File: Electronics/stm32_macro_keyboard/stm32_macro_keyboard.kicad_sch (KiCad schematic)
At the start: 37 parts, among them J1 USB_B_Micro, J2 Conn_01x04_Pin, SW1 SW_SPDT, U1 STM32F072CBTx, U2 AMS1117-3.3, Y1 16 MHz

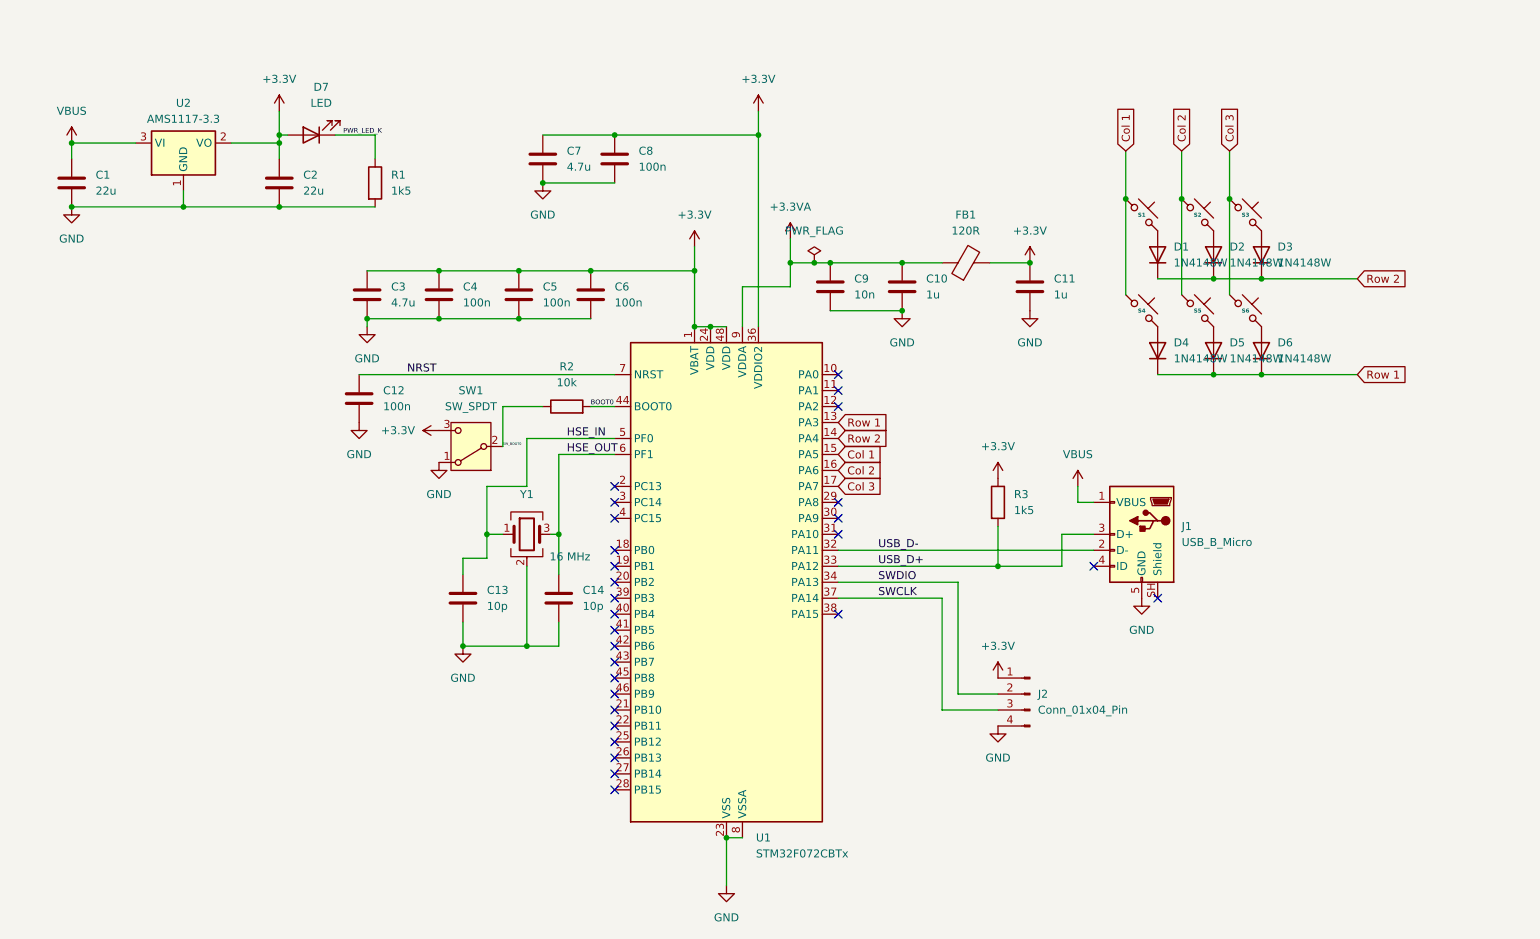
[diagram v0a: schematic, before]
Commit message: Finish schematic, tidy layout, and start STM32F103C8TX firmware
Schematic editing is complete; footprint assignment and PCB layout
are next. New CubeIDE project targets STM32F103C8TX replacing the
old STM32F072 MCU (see archive/stm32f072cbtx-mcu for the prior
STM32F0-based progress).

Co-Authored-By: Claude Sonnet 5 <noreply@anthropic.com>
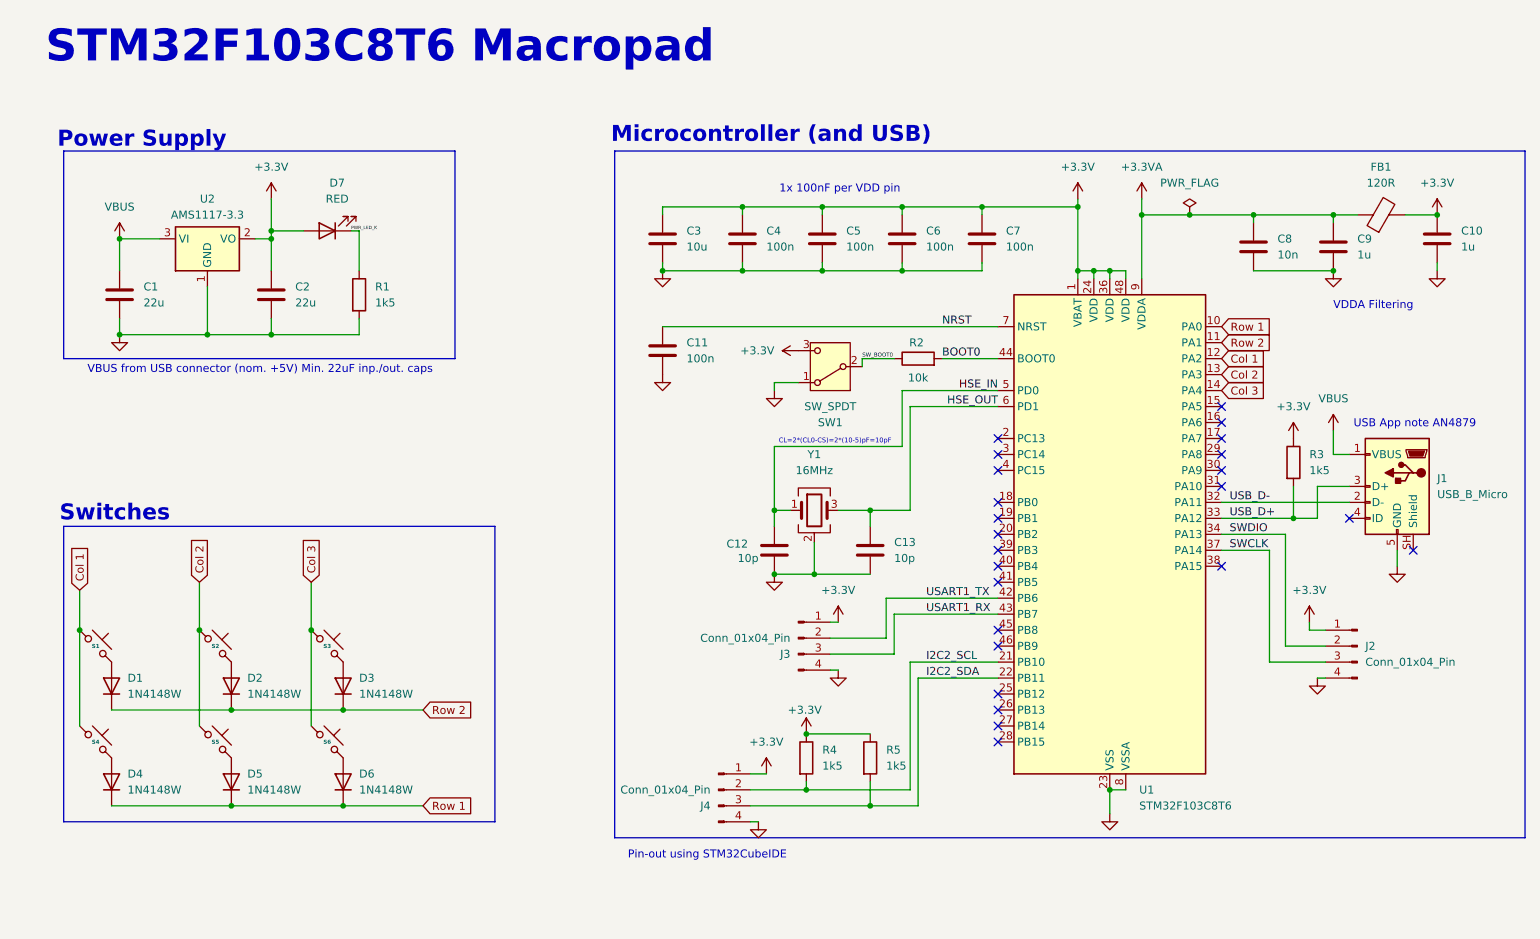
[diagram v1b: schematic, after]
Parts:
- removed C14: 10p, Capacitor_SMD:C_0402_1005Metric, symbol Device:C
- removed U1: STM32F072CBTx, Package_QFP:LQFP-48_7x7mm_P0.5mm, symbol MCU_ST_STM32F0:STM32F072CBTx
- added J3, J4: Conn_01x04_Pin, symbol Connector:Conn_01x04_Pin
- added R4, R5: 1k5, symbol Device:R
- added U1: STM32F103C8T6, Package_QFP:LQFP-48_7x7mm_P0.5mm, symbol MCU_ST_STM32F1:STM32F103C8Tx
- C1, C2: footprint Capacitor_SMD:C_0805_2012Metric -> (none)
- C10, C13, C4, C5, C6: footprint Capacitor_SMD:C_0402_1005Metric -> (none)
- C11: value 1u -> 100n; footprint Capacitor_SMD:C_0402_1005Metric -> (none)
- C12: value 100n -> 10p; footprint Capacitor_SMD:C_0402_1005Metric -> (none)
- C3: value 4.7u -> 10u; footprint Capacitor_SMD:C_0603_1608Metric -> (none)
- C7: value 4.7u -> 100n; footprint Capacitor_SMD:C_0603_1608Metric -> (none)
- C8: value 100n -> 10n; footprint Capacitor_SMD:C_0402_1005Metric -> (none)
- C9: value 10n -> 1u; footprint Capacitor_SMD:C_0402_1005Metric -> (none)
- D7: value LED -> RED; footprint LED_SMD:LED_0603_1608Metric -> (none)
- FB1: footprint Inductor_SMD:L_0603_1608Metric -> (none)
- J1: footprint Connector_USB:USB_Micro-B_Wuerth_629105150521 -> (none)
- J2: footprint Connector_PinHeader_2.54mm:PinHeader_1x04_P2.54mm_Vertical -> (none)
- R1, R2, R3: footprint Resistor_SMD:R_0402_1005Metric -> (none)
- SW1: footprint Button_Switch_SMD:SW_SPDT_PCM12 -> (none)
- Y1: value 16 MHz -> 16MHz; footprint Crystal:Crystal_SMD_3225-4Pin_3.2x2.5mm -> (none)
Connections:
- net +3.3V: now also C10.1, J3.1 (Pin_1), J4.1 (Pin_1), R4.1, R5.1, U1.1 (VBAT), U1.24 (VDD), U1.36 (VDD), U1.48 (VDD); no longer C11.1, C8.1
- net +3.3VA: now also C8.1, U1.9 (VDDA); no longer C10.1
- net BOOT0: now also U1.44 (BOOT0)
- net Col 1: now also U1.12 (PA2)
- net Col 2: now also U1.13 (PA3)
- net Col 3: now also U1.14 (PA4)
- net GND: now also J3.4 (Pin_4), J4.4 (Pin_4), U1.23 (VSS), U1.35 (VSS), U1.47 (VSS), U1.8 (VSSA)
- net HSE_IN: now also C12.1, U1.5 (PD0); no longer C13.1
- net HSE_OUT: now also C13.1, U1.6 (PD1)
- net NRST: now also C11.1, U1.7 (NRST); no longer C12.1
- net Row 1: now also U1.10 (PA0)
- net Row 2: now also U1.11 (PA1)
- net SWCLK: now also U1.37 (PA14)
- net SWDIO: now also U1.34 (PA13)
- net USB_D+: now also U1.33 (PA12)
- net USB_D-: now also U1.32 (PA11)
- new net I2C2_SCL: J4.2 (Pin_2), R4.2, U1.21 (PB10)
- new net I2C2_SDA: J4.3 (Pin_3), R5.2, U1.22 (PB11)
- new net USART1_RX: J3.3 (Pin_3), U1.43 (PB7)
- new net USART1_TX: J3.2 (Pin_2), U1.42 (PB6)
- no-connect marks 28 -> 24
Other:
- note added: "1x 100nF per VDD pin"
- note added: "CL=2*(CL0-CS)=2*(10-5)pF=10pF"
- note added: "Microcontroller (and USB)"
- note added: "Pin-out using STM32CubeIDE"
- note added: "Power Supply"
- note added: "STM32F103C8T6 Macropad"
- note added: "Switches"
- note added: "USB App note AN4879"
- note added: "VBUS from USB connector (nom. +5V) Min. 22uF inp./out. caps"
- note added: "VDDA Filtering"
- company: (none) -> Misbah
- title: (none) -> STM32F103C8T6 Macropad
- moved on the sheet: D1, D2, D3, D4, D5, D6, S1, S2, S3, S4, S5, S6
